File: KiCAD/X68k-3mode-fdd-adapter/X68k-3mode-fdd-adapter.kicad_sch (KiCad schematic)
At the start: 50 parts, among them J1 Conn_02x17_Odd_Even, J2 Conn_02x17_Odd_Even, J3 Conn_01x04, J4 Conn_01x04, J5 Conn_01x02_Pin, J6 Conn_01x04, J7 Conn_01x05_Pin, J8 Conn_01x05_Pin, Q1 2SC4213, SW1 SW_DIP_x04, U1 CH32V003F4U6, U2 74HC14, U3 74HC14, U4 74HC153, U5 74HC153, U6 ULN2003A

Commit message: 一通り配線した(未チェック)
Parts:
- removed J7, J8: Conn_01x05_Pin, Connector_PinHeader_1.27mm:PinHeader_1x05_P1.27mm_Vertical, symbol Connector:Conn_01x05_Pin
- removed R11: 1K, Resistor_SMD:R_0603_1608Metric, symbol Device:R_Small_US
- removed U2, U3: 74HC14, Package_SO:SO-14_5.3x10.2mm_P1.27mm, symbol 74xx:74HC14
- added SW2: SW_SPDT, Connector_PinHeader_2.54mm:PinHeader_1x03_P2.54mm_Vertical, symbol Switch:SW_SPDT
- added TP6: TestPoint, TestPoint:TestPoint_Pad_1.0x1.0mm, symbol Connector:TestPoint
- BZ1: footprint Buzzer_Beeper:Buzzer_12x9.5RM7.6 -> x68k-lib:UGCT7525AN4
- J1: footprint Connector_IDC:IDC-Header_2x17_P2.54mm_Vertical -> x68k-lib:PinHeader_2x17_P2.54mm_Horizontal_Mirror
- J2: footprint Connector_IDC:IDC-Header_2x17_P2.54mm_Vertical -> x68k-lib:PinSocket_2x17_P2.54mm_Horizontal_Mirror
- J6: footprint Connector_PinHeader_2.54mm:PinHeader_1x04_P2.54mm_Vertical -> Connector_PinSocket_2.54mm:PinSocket_1x04_P2.54mm_Vertical
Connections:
- net DRIVE_SELECT_0_BUF is gone; now on net DRIVE_SELECT_0: U5.6 (I0a)
- net DRIVE_SELECT_1_BUF is gone; now on net DRIVE_SELECT_1: U5.5 (I1a)
- net DRIVE_SELECT_2_BUF is gone; now on net DRIVE_SELECT_2: U5.4 (I2a)
- net DRIVE_SELECT_3_BUF is gone; now on net DRIVE_SELECT_3: U5.3 (I3a)
- net EJECT_BUF is gone; now on net EJECT: U1.19 (PD5)
- net EJECT_MASK_BUF is gone; now on net EJECT_MASK: U1.18 (PD4)
- net LED_BLINK_BUF is gone; now on net LED_BLINK: U1.20 (PD6)
- net OPTION_SELECT_0_BUF is gone; now on net OPTION_SELECT_0: U4.13 (I3b), U4.6 (I0a)
- net OPTION_SELECT_1_BUF is gone; now on net OPTION_SELECT_1: U4.10 (I0b), U4.5 (I1a)
- net OPTION_SELECT_2_BUF is gone; now on net OPTION_SELECT_2: U4.11 (I1b), U4.4 (I2a)
- net OPTION_SELECT_3_BUF is gone; now on net OPTION_SELECT_3: U4.12 (I2b), U4.3 (I3a)
- net READY: now also SW2.2 (B); no longer J2.34 (Pin_34), U6.16 (O1)
- net OPTION_SELECT_MAIN renamed OPTION_SELECT
- net OPTION_SELECT_SUB renamed OPTION_SELECT_PAIR
- new net DISK_CHANGE: J2.34 (Pin_34), SW2.3 (C), TP6.1
- new net READY_GEN_BUF: SW2.1 (A), U6.16 (O1)
- no-connect marks 9 -> 13
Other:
- moved on the sheet: R12, R5, R6, R7, R8

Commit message: 一通りの配線、調整を入れたバージョン
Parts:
- removed JP1, JP2: Jumper_2_Small_Open, Jumper:SolderJumper-2_P1.3mm_Open_RoundedPad1.0x1.5mm, symbol Jumper:Jumper_2_Small_Open
- removed JP3: Jumper_2_Bridged, Jumper:SolderJumper-2_P1.3mm_Bridged_RoundedPad1.0x1.5mm, symbol Jumper:Jumper_2_Bridged
- removed R15, R16: 10K, Resistor_SMD:R_0603_1608Metric, symbol Device:R_Small_US
- removed R17: 0, Resistor_SMD:R_0603_1608Metric, symbol Device:R_Small_US
- removed SW1: SW_DIP_x04, Button_Switch_SMD:SW_DIP_SPSTx04_Slide_Copal_CHS-04A_W5.08mm_P1.27mm_JPin, symbol Switch:SW_DIP_x04
- removed TP5, TP6: TestPoint, TestPoint:TestPoint_Pad_1.0x1.0mm, symbol Connector:TestPoint
- added C1: 10uF, Capacitor_SMD:C_0603_1608Metric, symbol Device:C_Small
- added C2, C3, C4, C5: 0.1uF, Capacitor_SMD:C_0603_1608Metric, symbol Device:C_Small
- added J7: Conn_01x03_Pin, Connector_PinHeader_2.54mm:PinHeader_1x03_P2.54mm_Vertical, symbol Connector:Conn_01x03_Pin
- added P1: USB_C_Plug_USB2.0, Connector_USB:USB_C_Receptacle_GCT_USB4125-xx-x-0190_6P_TopMnt_Horizontal, symbol Connector:USB_C_Receptacle_PowerOnly_6P
- added R31, R32: 5.1k, Resistor_SMD:R_0603_1608Metric, symbol Device:R_Small_US
- added SW1: SW_DIP_x02, Button_Switch_SMD:SW_DIP_SPSTx02_Slide_Copal_CHS-02A_W5.08mm_P1.27mm_JPin, symbol Switch:SW_DIP_x02
- D1: value WS2812B -> FDD ACCESS
- D2: value WS2812B -> FDD EJECT
- J5: value Conn_01x02_Pin -> SDIO; now not fitted
- R24: renamed from R18; value 0 -> 10K
- R25: renamed from R19; value 0 -> 10K
- R26: renamed from R20; value 0 -> 10K
- R27: renamed from R21; value 0 -> 10K
- renumbered R1 to R0, R2 to R1, R6 to R10, R7 to R11, R8 to R12, R5 to R13, R3 to R2, R13 to R20, R14 to R21, R4 to R3, R10 to R5, R9 to R6, R12 to R7
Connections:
- net DIPSW_2 is gone; now on net DISK_IN_GEN: U1.5 (PD0)
- net DIPSW_3 is gone; now on net FDD_INT_GEN: U1.1 (PD7)
- net DISK_CHANGE is gone; now on net DISK_CHANGE_DOSV: J2.34 (Pin_34), SW2.3 (C)
- net FDD_INT is gone; now on net FDD_INT_BUF: J1.19 (Pin_19)
- net +5V: now also C1.1, C2.1, C3.1, C4.1, C5.1, J7.3 (Pin_3), P1.A9 (VBUS), P1.B9 (VBUS), SW1.3, SW1.4
- net BUZZER: now also U1.3 (PA2/OSC0)
- net DIPSW_0: now also SW1.1
- net DIPSW_1: now also SW1.2
- net GND: now also C1.2, C2.2, C3.2, C4.2, C5.2, J7.1 (Pin_1), P1.A12 (GND), P1.B12 (GND), P1.S1 (SHIELD), R31.2, R32.2
- net LED_DATA: now also D1.4 (DIN), J7.2 (Pin_2)
- net FDD_INT_BUF: now reaches U6.14 (O3)
- net FDD_INT_GEN: now reaches U6.3 (I3)
- net DISK_CHANGE_DOSV: now reaches J5.1 (Pin_1), U1.15 (PD1/SWIO)
- new net: P1.A5 (CC1), R31.1
- new net: P1.B5 (CC2), R32.1
- no-connect marks 13 -> 12
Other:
- moved on the sheet: R0, R1, R10, R11, R12, R13, R2, R3, R5, R6, R7

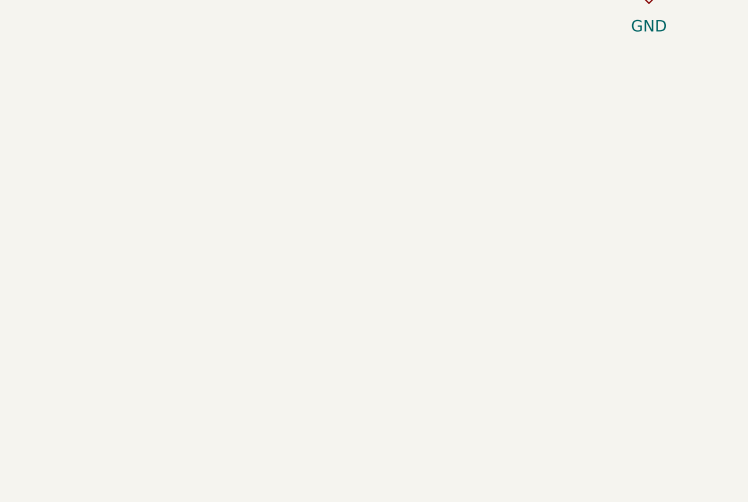
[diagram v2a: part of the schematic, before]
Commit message: 基板形状を見直した
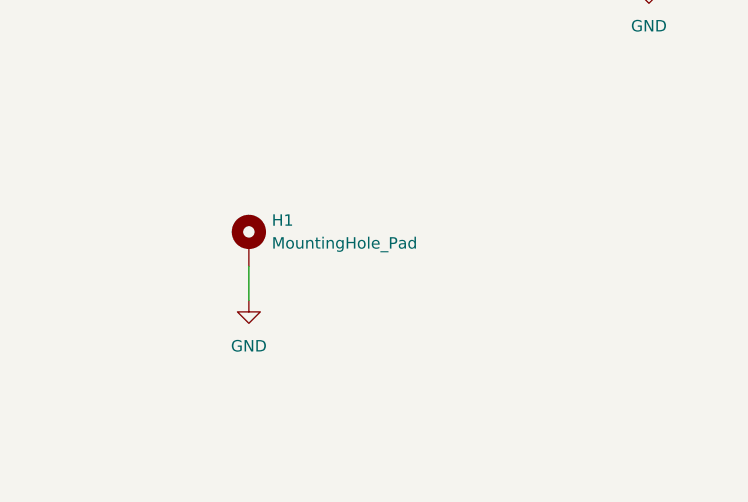
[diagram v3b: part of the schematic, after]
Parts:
- added H1: MountingHole_Pad, MountingHole:MountingHole_2.7mm_M2.5_Pad, symbol Mechanical:MountingHole_Pad
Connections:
- net GND: now also H1.1
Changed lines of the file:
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@@
 	(wire
 		(pts
+			(xy 34.29 254) (xy 34.29 257.81)
+		)
+		(stroke
+			(width 0)
+			(type default)
+		)
+	)
+	(wire
+		(pts
 			(xy 40.64 52.07) (xy 45.72 52.07)
 		)
@@
 	)
 	(symbol
+		(lib_id "Mechanical:MountingHole_Pad")
+		(at 34.29 251.46 0)
+		(unit 1)
+		(exclude_from_sim yes)
+		(in_bom no)
+		(on_board yes)
+		(dnp no)
+		(fields_autoplaced yes)
+		(property "Reference" "H1"
+			(at 36.83 248.9199 0)
+			(effects
+				(font
+					(size 1.27 1.27)
+				)
+				(justify left)
+			)
+		)
+		(property "Value" "MountingHole_Pad"
+			(at 36.83 251.4599 0)
+			(effects
+				(font
+					(size 1.27 1.27)
+				)
+				(justify left)
+			)
+		)
+		(property "Footprint" "MountingHole:MountingHole_2.7mm_M2.5_Pad"
+			(at 34.29 251.46 0)
+			(effects
+				(font
+					(size 1.27 1.27)
+				)
+				(hide yes)
+			)
+		)
+		(property "Datasheet" "~"
+			(at 34.29 251.46 0)
+			(effects
+				(font
+					(size 1.27 1.27)
+				)
+				(hide yes)
+			)
+		)
+		(property "Description" "Mounting Hole with connection"
+			(at 34.29 251.46 0)
+			(effects
+				(font
+					(size 1.27 1.27)
+				)
+				(hide yes)
+			)
+		)
+		(pin "1"
+		)
+		(instances
+			(project ""
+				(path "/13b3a4ee-84d6-44b3-962d-9cf7c36d7564"
+					(reference "H1")
+					(unit 1)
+				)
+			)
+		)
+	)
+	(symbol
 		(lib_id "Device:R_Small_US")
 		(at 66.04 71.12 0)
@@
 					(unit 1)
 				)
+			)
+		)
+	)
+	(symbol
+		(lib_id "power:GND")
+		(at 34.29 257.81 0)
+		(unit 1)
+		(exclude_from_sim no)
+		(in_bom yes)
+		(on_board yes)
+		(dnp no)
+		(fields_autoplaced yes)
+		(property "Reference" "#PWR053"
+			(at 34.29 264.16 0)
+			(effects
+				(font
+					(size 1.27 1.27)
+				)
+				(hide yes)
+			)
+		)
+		(property "Value" "GND"
+			(at 34.29 262.89 0)
+			(effects
+				(font
+					(size 1.27 1.27)
+				)
+			)
+		)
+		(property "Footprint" ""
+			(at 34.29 257.81 0)
+			(effects
+				(font
+					(size 1.27 1.27)
+				)
+				(hide yes)
+			)
+		)
+		(property "Datasheet" ""
+			(at 34.29 257.81 0)
+			(effects
+				(font
+					(size 1.27 1.27)
+				)
+				(hide yes)
+			)
+		)
+		(property "Description" "Power symbol creates a global label with name \"GND\" , ground"
+			(at 34.29 257.81 0)
+			(effects
+				(font
+					(size 1.27 1.27)
+				)
+				(hide yes)
+			)
+		)
+		(pin "1"
+		)
+		(instances
+			(project "X68k-3mode-fdd-adapter"
+				(path "/13b3a4ee-84d6-44b3-962d-9cf7c36d7564"
+					(reference "#PWR053")
+					(unit 1)
+				)

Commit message: v1.0.0注文版
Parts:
- removed D1: FDD ACCESS, LED_SMD:LED_WS2812B_PLCC4_5.0x5.0mm_P3.2mm, symbol LED:WS2812B
- removed D2: FDD EJECT, LED_SMD:LED_WS2812B_PLCC4_5.0x5.0mm_P3.2mm, symbol LED:WS2812B
- added D1, D2: SK6812MINI, x68k-lib:SK6812MINI-HS, symbol X68k-lib:SK6812MINI-HS
- D3: value D_Schottky -> SS2040FL; LCIC (none) -> C268712
- J1: LCIC (none) -> C725929
- J3: LCIC (none) -> C590635
- J4: value Conn_01x04 -> PH-4A; LCIC (none) -> C2321
- J7, SW2: LCIC (none) -> C49257
- P1: LCIC C456012 -> C168701
- Q1: value 2SC4213 -> 2SC2712; footprint Package_TO_SOT_SMD:SOT-323_SC-70 -> Package_TO_SOT_SMD:SOT-23
- SW1: footprint Button_Switch_SMD:SW_DIP_SPSTx02_Slide_Copal_CHS-02A_W5.08mm_P1.27mm_JPin -> Button_Switch_SMD:SW_DIP_SPSTx02_Slide_Copal_CHS-02B_W7.62mm_P1.27mm; LCIC (none) -> C49257
- TP4: now not fitted
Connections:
- net +5V: now also D1.3 (VDD), D2.3 (VDD)
- net GND: now also D1.1 (VSS), D2.1 (VSS)
- net LED_DATA: now also D1.2 (DIN)
- new net: D1.4 (DOUT), D2.2 (DIN)

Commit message: LCIC→LCSCに修正
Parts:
- D1, D2: LCIC C2922787 -> (none); LCSC (none) -> C2922787
- D3: LCIC C268712 -> (none); LCSC (none) -> C268712
- J1: LCIC C725929 -> (none); LCSC (none) -> C725929
- J3: LCIC C590635 -> (none); LCSC (none) -> C590635
- J4: LCIC C2321 -> (none); LCSC (none) -> C2321
- J7, SW2: LCIC C49257 -> (none); LCSC (none) -> C49257
- P1: LCIC C168701 -> (none); LCSC (none) -> C168701
- SW1: LCIC C49257 -> (none); LCSC (none) -> C3294661
- U4, U5: LCIC C53334 -> (none); LCSC (none) -> C53334
- U6: LCIC C411052 -> (none); LCSC (none) -> C411052
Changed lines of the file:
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@@
 			)
 		)
-		(property "LCIC" "C168701"
+		(property "LCSC" "C168701"
 			(at 44.45 77.47 90)
 			(effects
@@
 			)
 		)
-		(property "LCIC" "C49257"
+		(property "LCSC" "C3294661"
 			(at 287.02 35.56 0)
 			(effects
@@
 			)
 		)
-		(property "LCIC" "C2922787"
+		(property "LCSC" "C2922787"
 			(at 341.63 50.8 0)
 			(effects
@@
 			)
 		)
-		(property "LCIC" "C2321"
+		(property "LCSC" "C2321"
 			(at 50.8 46.99 0)
 			(effects
@@
 			)
 		)
-		(property "LCIC" "C411052"
+		(property "LCSC" "C411052"
 			(at 78.74 203.2 0)
 			(effects
@@
 			)
 		)
-		(property "LCIC" "C53334"
+		(property "LCSC" "C53334"
 			(at 276.86 129.54 0)
 			(effects
@@
 			)
 		)
-		(property "LCIC" "C53334"
+		(property "LCSC" "C53334"
 			(at 275.59 236.22 0)
 			(effects
@@
 			)
 		)
-		(property "LCIC" "C590635"
+		(property "LCSC" "C590635"
 			(at 25.4 46.99 0)
 			(effects
@@
 			)
 		)
-		(property "LCIC" "C725929"
+		(property "LCSC" "C725929"
 			(at 67.31 121.92 0)
 			(effects
@@
 			)
 		)
-		(property "LCIC" "C268712"
+		(property "LCSC" "C268712"
 			(at 90.17 33.02 90)
 			(effects
@@
 			)
 		)
-		(property "LCIC" "C49257"
+		(property "LCSC" "C49257"
 			(at 97.79 142.24 0)
 			(effects
@@
 			)
 		)
-		(property "LCIC" "C49257"
+		(property "LCSC" "C49257"
 			(at 336.55 27.94 0)
 			(effects
@@
 			)
 		)
-		(property "LCIC" "C2922787"
+		(property "LCSC" "C2922787"
 			(at 368.3 50.8 0)
 			(effects

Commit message: FDD側の2x17ピンソケット(フィメールヘッダ)のLCSC型番が判明したので入力した
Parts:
- J2: value Conn_02x17_Odd_Even -> Double Row 3A Copper Alloy 34P Female Headers (PM254-2-17-W-8.5); LCSC (none) -> C2897437
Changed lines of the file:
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@@
 			)
 		)
-		(property "Value" "Conn_02x17_Odd_Even"
+		(property "Value" "Double Row 3A Copper Alloy 34P Female Headers (PM254-2-17-W-8.5)"
 			(at 342.9 97.79 0)
 			(effects
@@
 			)
 		)
-		(property "Datasheet" "~"
+		(property "Datasheet" "https://wmsc.lcsc.com/wmsc/upload/file/pdf/v2/lcsc/2306091006_HCTL-PM254-2-17-W-8-5_C2897437.pdf"
 			(at 341.63 121.92 0)
 			(effects
@@
 			(at 341.63 121.92 0)
 			(effects
+				(font
+					(size 1.27 1.27)
+				)
+				(hide yes)
+			)
+		)
+		(property "LCSC" "C2897437"
+			(at 341.63 121.92 0)
+			(effects

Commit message: BuzzerシンボルをSpeakerシンボルに変更
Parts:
- BZ1: value Buzzer -> Speaker; symbol Device:Buzzer -> Device:Speaker
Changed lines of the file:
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@@
 	(wire
 		(pts
-			(xy 82.55 31.75) (xy 82.55 29.21)
+			(xy 255.27 254) (xy 250.19 254)
 		)
 		(stroke
@@
 	(wire
 		(pts
-			(xy 255.27 254) (xy 250.19 254)
+			(xy 74.93 62.23) (xy 52.07 62.23)
 		)
 		(stroke
@@
 	(wire
 		(pts
-			(xy 74.93 62.23) (xy 52.07 62.23)
+			(xy 158.75 157.48) (xy 173.99 157.48)
 		)
 		(stroke
@@
 	(wire
 		(pts
-			(xy 158.75 157.48) (xy 173.99 157.48)
+			(xy 165.1 184.15) (xy 165.1 186.69)
 		)
 		(stroke
@@
 	(wire
 		(pts
-			(xy 165.1 184.15) (xy 165.1 186.69)
+			(xy 168.91 184.15) (xy 168.91 186.69)
 		)
 		(stroke
@@
 	(wire
 		(pts
-			(xy 168.91 184.15) (xy 168.91 186.69)
+			(xy 82.55 29.21) (xy 82.55 33.02)
 		)
 		(stroke
@@
 	(wire
 		(pts
+			(xy 82.55 35.56) (xy 82.55 36.83)
+		)
+		(stroke
+			(width 0)
+			(type default)
+		)
+	)
+	(wire
+		(pts
 			(xy 158.75 110.49) (xy 175.26 110.49)
 		)
@@
 	)
 	(symbol
-		(lib_id "Device:Buzzer")
-		(at 80.01 34.29 0)
+		(lib_id "Device:Speaker")
+		(at 77.47 33.02 0)
 		(mirror y)
 		(unit 1)
@@
 		(fields_autoplaced yes)
 		(property "Reference" "BZ1"
-			(at 79.2549 26.67 0)
+			(at 76.962 24.13 0)
 			(effects
 				(font
@@
 			)
 		)
-		(property "Value" "Buzzer"
-			(at 79.2549 29.21 0)
+		(property "Value" "Speaker"
+			(at 76.962 26.67 0)
 			(effects
 				(font
@@
 		)
 		(property "Footprint" "x68k-lib:UGCT7525AN4"
-			(at 80.645 31.75 90)
+			(at 77.47 38.1 0)
 			(effects
 				(font
@@
 		)
 		(property "Datasheet" "~"
-			(at 80.645 31.75 90)
+			(at 77.724 34.29 0)
 			(effects
 				(font
@@
 			)
 		)
-		(property "Description" "Buzzer, polarized"
-			(at 80.01 34.29 0)
+		(property "Description" "Speaker"
+			(at 77.47 33.02 0)
 			(effects
 				(font
